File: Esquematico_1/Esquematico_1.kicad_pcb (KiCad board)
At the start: 6 copper layers, 40.7 x 40.7 mm, 94 parts, among them IC1 AP2112K-3.3TRG1, J1 Screw_Terminal_01x04, J2 Screw_Terminal_01x03, J3 Screw_Terminal_01x06, J4 Screw_Terminal_01x08, J5 SWD, J6 Screw_Terminal_01x04, J7 USB_C_Receptacle_USB2.0_16P, J8 Screw_Terminal_01x01, J9 Screw_Terminal_01x01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

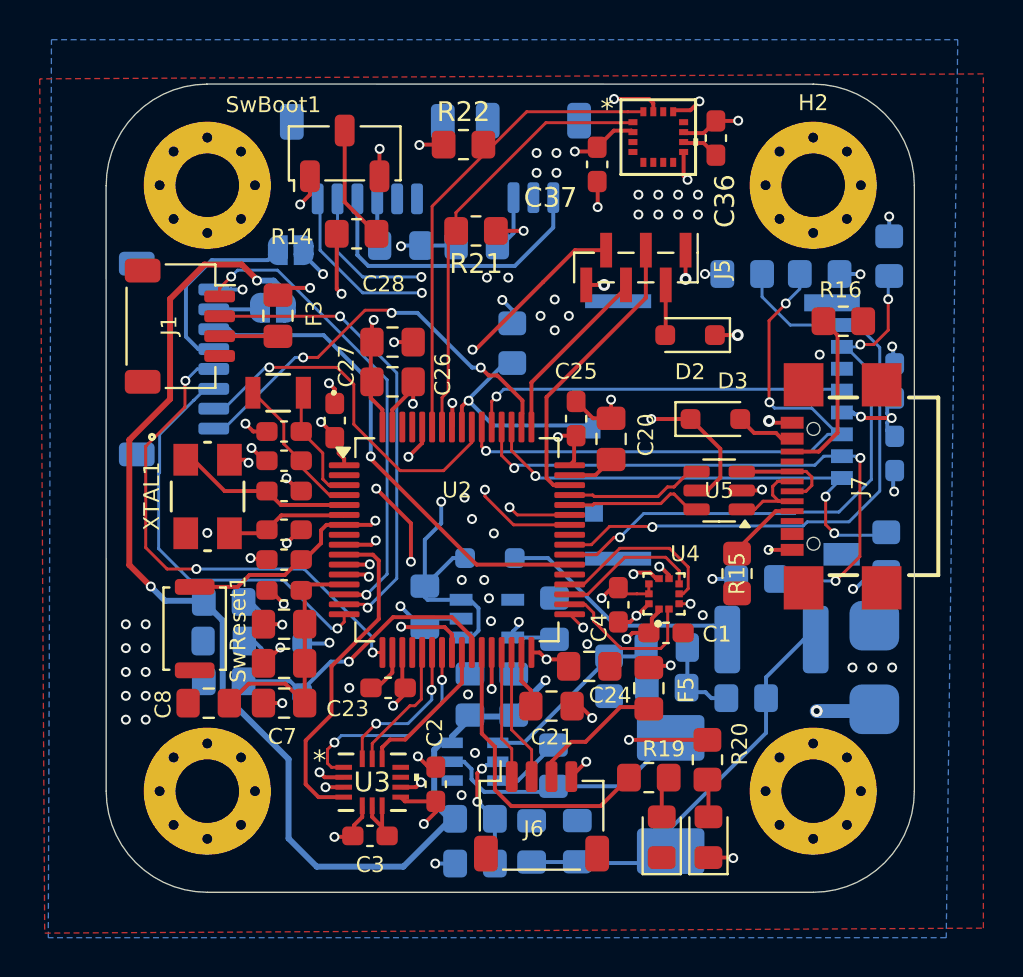
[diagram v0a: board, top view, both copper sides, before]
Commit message: Pequeños cambios en los silkscreen
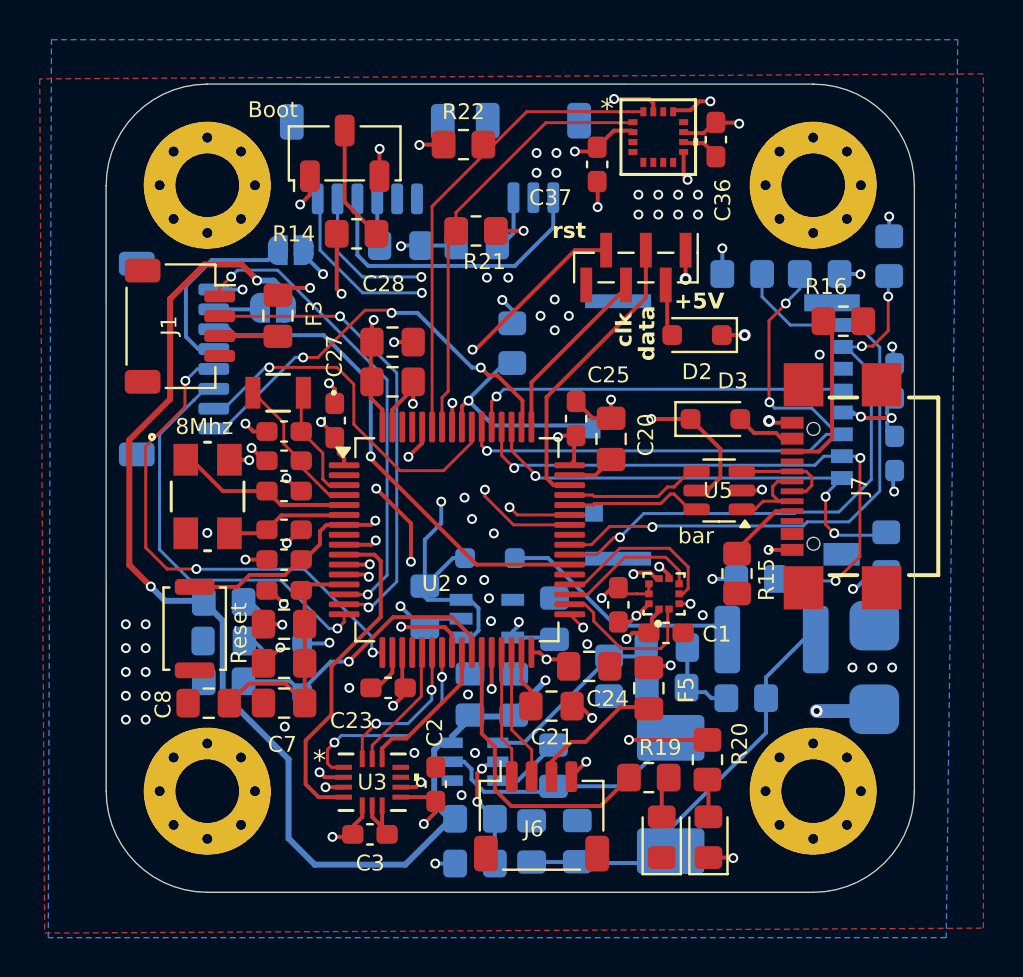
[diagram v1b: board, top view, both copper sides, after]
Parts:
- moved D2 0.35 mm to (116.5, 81.6)
- moved C3 0.08 mm to (100.0, 106.7)
- moved C36 0.08 mm to (117.4, 71.7)
- renumbered XTAL1 to 8Mhz, SwBoot1 to Boot, SwReset1 to Reset, U4 to bar
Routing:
- net GND: track 55.7 -> 52.9 mm, vias 81 -> 80
- net +3V3: track 56.7 -> 57.8 mm
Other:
- board text added: "+5V"
- board text added: "clk"
- board text added: "data"
- board text added: "rst"

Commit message: Silkscreen y huellas en general de la imagenes
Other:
- board text added: "Hernán Ibarra"
- board text added: "Lucas Garcia"
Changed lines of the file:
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@@
 		(tags "resistor handsolder")
 		(property "Reference" "R10"
-			(at -3.3 0.025 0)
+			(at -3.225 -0.9925 0)
 			(layer "B.SilkS")
 			(effects
@@
 		)
 	)
+	(gr_text "Lucas Garcia "
+		(at 101.325 108.7825 0)
+		(layer "B.SilkS")
+		(effects
+			(font
+				(size 0.8 0.8)
+				(thickness 0.15)
+				(bold yes)
+			)
+			(justify left bottom mirror)
+		)
+	)
+	(gr_text "Hernán Ibarra"
+		(at 111.925 70.0325 180)
+		(layer "B.SilkS")
+		(effects
+			(font
+				(size 0.8 0.8)
+				(thickness 0.15)
+				(bold yes)
+			)
+			(justify left bottom mirror)
+		)
+	)

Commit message: crow
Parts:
- added G***: LOGO, images:crow3, F.Cu at (96.9, 92.1)

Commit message: crow final
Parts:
- moved G*** 2.88 mm to (97.6, 89.3)

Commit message: Correccion final
2 hermana
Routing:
- net GND: track 52.9 -> 51.4 mm, vias 80 -> 84

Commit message: error fixed
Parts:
- renumbered Boot to SwBoot1, Reset to SwReset1, bar to U4, 8Mhz to XTAL1
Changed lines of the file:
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@@
 		(at 91.84 89.7)
 		(tags "ECS-80-12-30BQ-JES-TR ")
-		(property "Reference" "8Mhz"
+		(property "Reference" "XTAL1"
 			(at -0.165 -3.5175 0)
 			(unlocked yes)
@@
 		(sheetname "/MCU/")
 		(sheetfile "microcontrolador.kicad_sch")
-		(attr smd)
+		(attr smd exclude_from_bom)
 		(fp_line
 			(start -1.8288 -0.734663)
@@
 		(sheetname "/Sensores/")
 		(sheetfile "sensores_.kicad_sch")
-		(attr smd)
+		(attr smd exclude_from_bom)
 		(fp_line
 			(start -0.227064 -0.735)
@@
 		(sheetname "/Sensores/")
 		(sheetfile "sensores_.kicad_sch")
-		(attr smd)
+		(attr smd exclude_from_bom)
 		(fp_line
 			(start -0.227064 0.735)
@@
 		(sheetname "/MCU/")
 		(sheetfile "microcontrolador.kicad_sch")
-		(attr smd)
+		(attr smd exclude_from_bom)
 		(fp_line
 			(start -0.227064 0.735)
@@
 			)
 		)
-		(property "LCSC Part Name" "C965812"
+		(property "LCSC Part Name" "C965815"
 			(at 0 0 90)
 			(unlocked yes)
@@
 		(sheetname "/MCU/")
 		(sheetfile "microcontrolador.kicad_sch")
-		(attr smd)
+		(attr smd exclude_from_bom)
 		(fp_line
 			(start -0.261252 -0.735)
@@
 		(sheetname "/MCU/")
 		(sheetfile "microcontrolador.kicad_sch")
-		(attr smd)
+		(attr smd exclude_from_bom)
 		(fp_line
 			(start -0.227064 0.735)
@@
 		(sheetname "/JST y CAM/")
 		(sheetfile "jst_cam.kicad_sch")
-		(attr smd)
+		(attr smd exclude_from_bom)
 		(fp_line
 			(start -0.745 3.11)
@@
 		(layer "F.Cu")
 		(at 114.815 94.6 90)
-		(property "Reference" "bar"
+		(property "Reference" "U4"
 			(at 2.9175 1.61 180)
 			(layer "F.SilkS")
@@
 		(descr "Slide Switch, SMD, Nidec CAS series, https://www.nidec-components.com/e/catalog/switch/cas.pdf")
 		(tags "SMD slide switch Nidec CAS 120A ")
-		(property "Reference" "Boot"
+		(property "Reference" "SwBoot1"
 			(at 2.195 -3.615 0)
 			(unlocked yes)
@@
 		(sheetname "/JST y CAM/")
 		(sheetfile "jst_cam.kicad_sch")
-		(attr through_hole)
+		(attr through_hole exclude_from_bom)
 		(fp_line
 			(start -3.2 -4.8)
@@
 		(descr "http://www.alps.com/prod/info/E/HTML/Tact/SurfaceMount/SKRK/SKRKAHE020.html")
 		(tags "SMD SMT button")
-		(property "Reference" "Reset"
+		(property "Reference" "SwReset1"
 			(at -0.2325 2.235 90)
 			(layer "F.SilkS")
@@
 		(sheetname "/MCU/")
 		(sheetfile "microcontrolador.kicad_sch")
-		(attr smd)
+		(attr smd exclude_from_bom)
 		(fp_line
 			(start -0.227064 -0.735)
@@
 		(sheetname "/MCU/")
 		(sheetfile "microcontrolador.kicad_sch")
-		(attr smd)
+		(attr smd exclude_from_bom)
 		(fp_line
 			(start -0.227064 -0.735)
@@
 		(sheetname "/MCU/")
 		(sheetfile "microcontrolador.kicad_sch")
-		(attr smd)
+		(attr smd exclude_from_bom)
 		(fp_line
 			(start -0.227064 -0.735)
@@
 		(sheetname "/JST y CAM/")
 		(sheetfile "jst_cam.kicad_sch")
-		(attr exclude_from_pos_files)
+		(attr exclude_from_pos_files exclude_from_bom)
 		(fp_line
 			(start 1.45 1.45)
@@
 		(sheetname "/JST y CAM/")
 		(sheetfile "jst_cam.kicad_sch")
-		(attr exclude_from_pos_files)
+		(attr exclude_from_pos_files exclude_from_bom)
 		(fp_line
 			(start 1.45 1.45)
@@
 		(sheetname "/MCU/")
 		(sheetfile "microcontrolador.kicad_sch")
-		(attr smd)
+		(attr smd exclude_from_bom)
 		(fp_line
 			(start -0.227064 0.735)
@@
 		(sheetname "/MCU/")
 		(sheetfile "microcontrolador.kicad_sch")
-		(attr smd)
+		(attr smd exclude_from_bom)
 		(fp_line
 			(start -0.227064 0.735)
@@
 		(sheetname "/MCU/")
 		(sheetfile "microcontrolador.kicad_sch")
-		(attr smd)
+		(attr smd exclude_from_bom)
 		(fp_line
 			(start -0.227064 -0.735)
@@
 		(sheetname "/PowerMangment/")
 		(sheetfile "power.kicad_sch")
-		(attr smd)
+		(attr smd exclude_from_bom)
 		(fp_line
 			(start -3.66 3.41)

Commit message: USB fix
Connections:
- J7 pad A4: (no net) -> Net-(D3-A)
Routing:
- net Net-(D3-A): track 3.02 -> 9.83 mm
- net /JST y CAM/CC2: track 8.36 -> 13.1 mm, vias 0 -> 2
- net SDIO_D2: track 24.5 -> 23.4 mm

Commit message: ultimo retoque final
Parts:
- moved C23 0.17 mm to (100.8, 99.3)
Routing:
- net GND: track 51.4 -> 45.5 mm, vias 84 -> 88
- net ESC1: track 20.5 -> 21.1 mm
